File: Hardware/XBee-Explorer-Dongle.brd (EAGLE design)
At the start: 40.6 x 27.9 mm, 37 parts, among them U2 XBEE-1B3, U3 MIC5219 3.3V, U4 FTS31XS-U

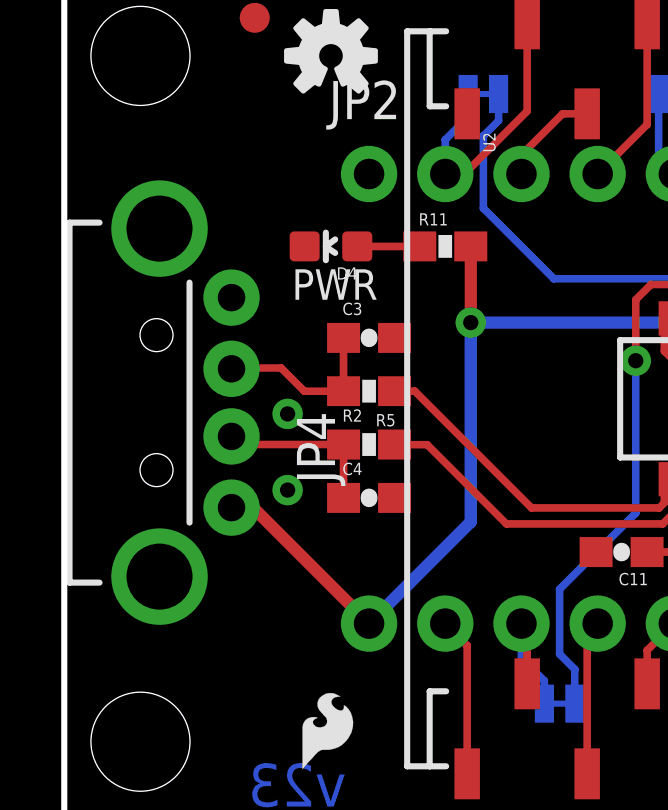
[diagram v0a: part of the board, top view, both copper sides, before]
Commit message: Fixed USB alignment issue.
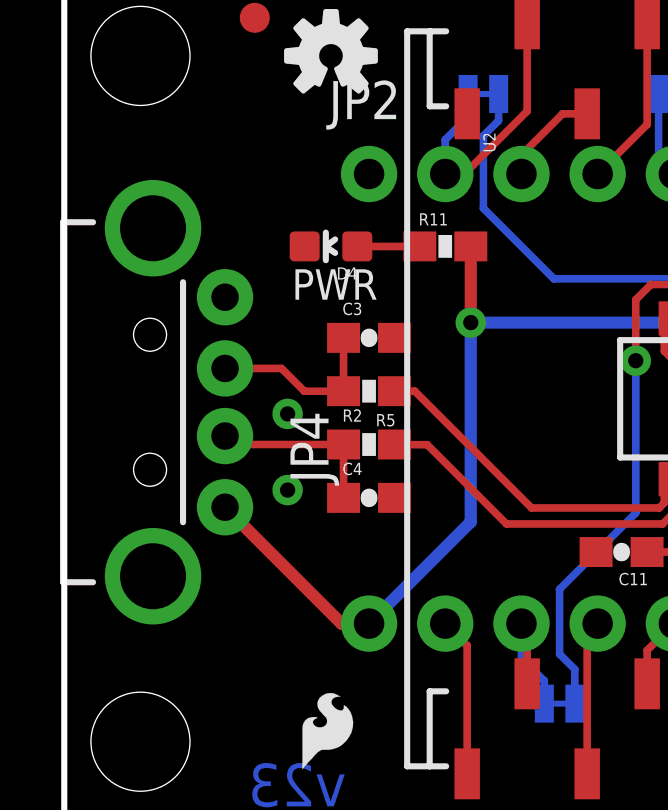
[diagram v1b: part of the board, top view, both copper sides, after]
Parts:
- moved JP4 0.22 mm to (2.96, 13.9)
